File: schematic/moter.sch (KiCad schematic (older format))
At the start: 8 parts, among them J8 Conn_01x05, J9 Conn_01x05, U3 PCA9685PW

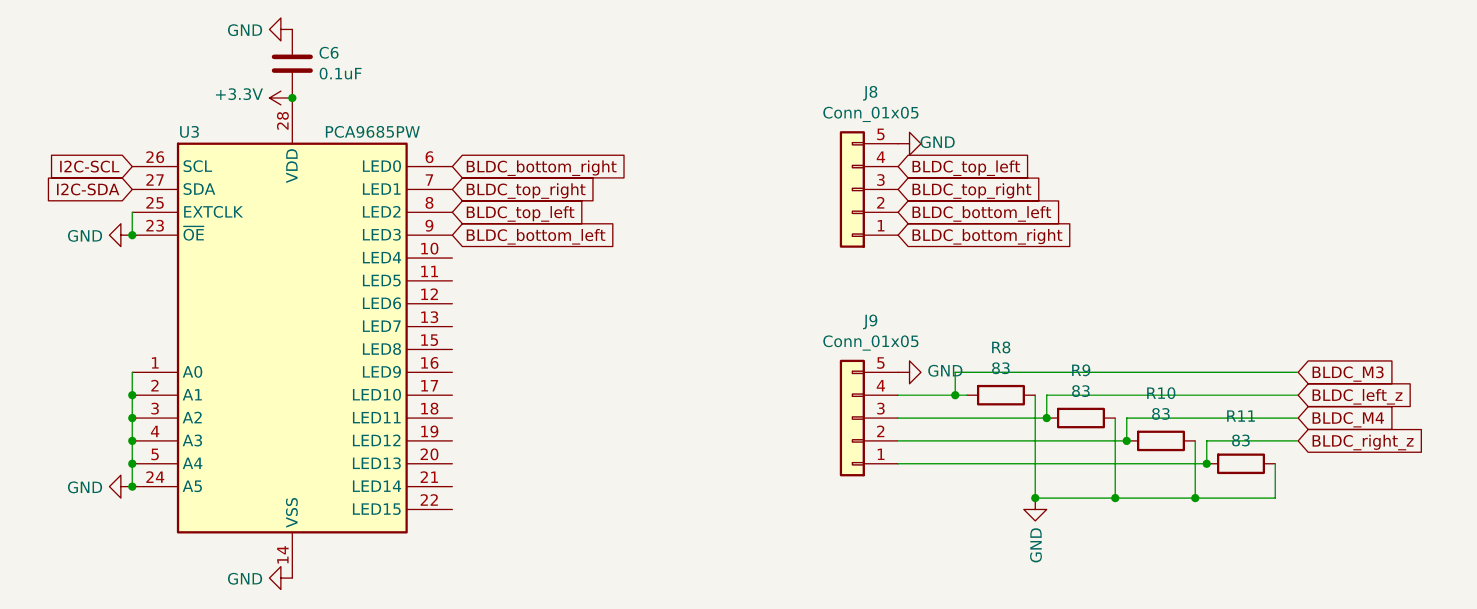
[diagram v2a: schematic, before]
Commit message: boost converter on Apsu board and PCB design
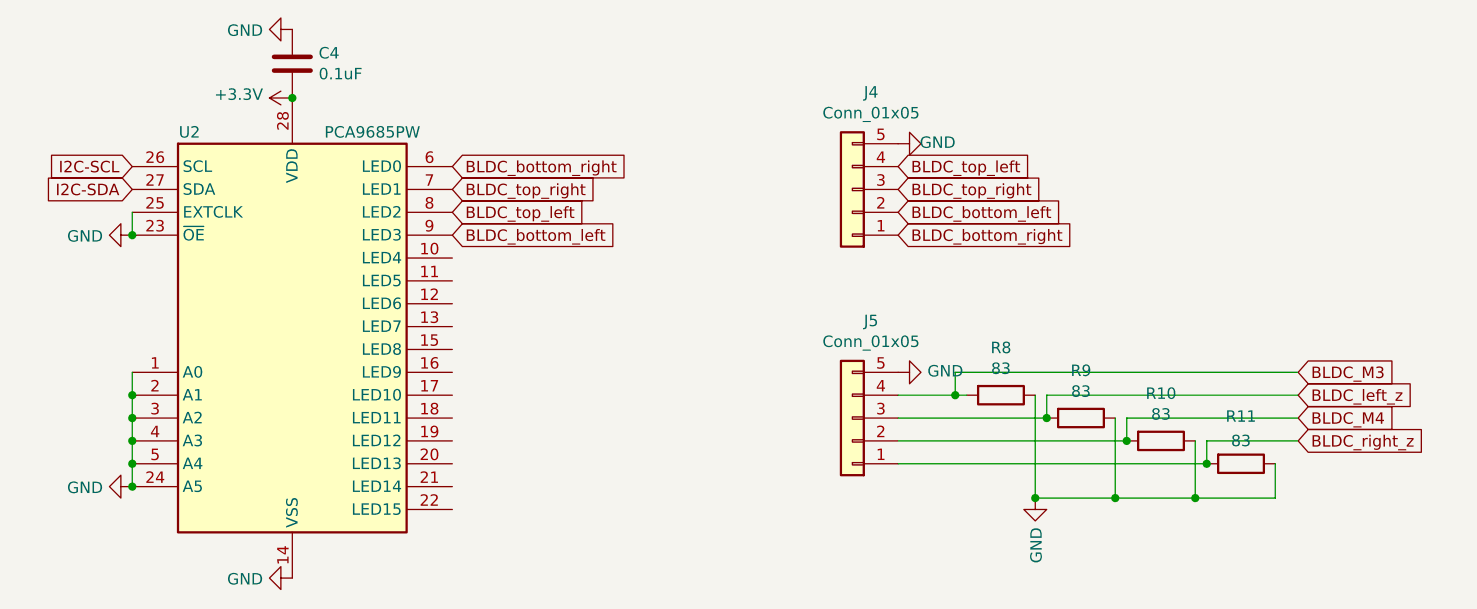
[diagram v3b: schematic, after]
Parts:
- renumbered C6 to C4, J8 to J4, J9 to J5, U3 to U2
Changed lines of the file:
@@
 $Descr A4 11693 8268
 encoding utf-8
-Sheet 4 5
+Sheet 3 5
 Title ""
 Date ""
@@
 P 2400 2550
 AR Path="/5EF432FA" Ref="U?"  Part="1"
-AR Path="/5EF07089/5EF432FA" Ref="U3"  Part="1"
-F 0 "U3" H 1950 3400 50  0000 C CNN
+AR Path="/5EF07089/5EF432FA" Ref="U2"  Part="1"
+F 0 "U2" H 1950 3400 50  0000 C CNN
 F 1 "PCA9685PW" H 2750 3400 50  0000 C CNN
 F 2 "Package_SO:TSSOP-28_4.4x9.7mm_P0.65mm" H 2425 1575 50  0001 L CNN
@@
 P 2400 1550
 AR Path="/5EF43302" Ref="#PWR?"  Part="1"
-AR Path="/5EF07089/5EF43302" Ref="#PWR031"  Part="1"
-F 0 "#PWR031" H 2400 1400 50  0001 C CNN
+AR Path="/5EF07089/5EF43302" Ref="#PWR022"  Part="1"
+F 0 "#PWR022" H 2400 1400 50  0001 C CNN
 F 1 "+3.3V" V 2415 1678 50  0000 L CNN
 F 2 "" H 2400 1550 50  0001 C CNN
@@
 P 2400 1400
 AR Path="/5EF43308" Ref="C?"  Part="1"
-AR Path="/5EF07089/5EF43308" Ref="C6"  Part="1"
-F 0 "C6" H 2515 1446 50  0000 L CNN
+AR Path="/5EF07089/5EF43308" Ref="C4"  Part="1"
+F 0 "C4" H 2515 1446 50  0000 L CNN
 F 1 "0.1uF" H 2515 1355 50  0000 L CNN
 F 2 "Capacitor_SMD:C_0805_2012Metric_Pad1.15x1.40mm_HandSolder" H 2438 1250 50  0001 C CNN
@@
 P 2400 3650
 AR Path="/5EF4330F" Ref="#PWR?"  Part="1"
-AR Path="/5EF07089/5EF4330F" Ref="#PWR032"  Part="1"
-F 0 "#PWR032" H 2400 3400 50  0001 C CNN
+AR Path="/5EF07089/5EF4330F" Ref="#PWR023"  Part="1"
+F 0 "#PWR023" H 2400 3400 50  0001 C CNN
 F 1 "GND" V 2405 3522 50  0000 R CNN
 F 2 "" H 2400 3650 50  0001 C CNN
@@
 P 1700 3250
 AR Path="/5EF4331F" Ref="#PWR?"  Part="1"
-AR Path="/5EF07089/5EF4331F" Ref="#PWR029"  Part="1"
-F 0 "#PWR029" H 1700 3000 50  0001 C CNN
+AR Path="/5EF07089/5EF4331F" Ref="#PWR020"  Part="1"
+F 0 "#PWR020" H 1700 3000 50  0001 C CNN
 F 1 "GND" V 1705 3122 50  0000 R CNN
 F 2 "" H 1700 3250 50  0001 C CNN
@@
 P 1700 2150
 AR Path="/5EF43326" Ref="#PWR?"  Part="1"
-AR Path="/5EF07089/5EF43326" Ref="#PWR028"  Part="1"
-F 0 "#PWR028" H 1700 1900 50  0001 C CNN
+AR Path="/5EF07089/5EF43326" Ref="#PWR019"  Part="1"
+F 0 "#PWR019" H 1700 1900 50  0001 C CNN
 F 1 "GND" V 1705 2022 50  0000 R CNN
 F 2 "" H 1700 2150 50  0001 C CNN
@@
 P 2400 1250
 AR Path="/5EF4332D" Ref="#PWR?"  Part="1"
-AR Path="/5EF07089/5EF4332D" Ref="#PWR030"  Part="1"
-F 0 "#PWR030" H 2400 1000 50  0001 C CNN
+AR Path="/5EF07089/5EF4332D" Ref="#PWR021"  Part="1"
+F 0 "#PWR021" H 2400 1000 50  0001 C CNN
 F 1 "GND" V 2405 1122 50  0000 R CNN
 F 2 "" H 2400 1250 50  0001 C CNN
@@
 P 5050 2750
 AR Path="/5EF64F4D" Ref="#PWR?"  Part="1"
-AR Path="/5EF07089/5EF64F4D" Ref="#PWR033"  Part="1"
-F 0 "#PWR033" H 5050 2500 50  0001 C CNN
+AR Path="/5EF07089/5EF64F4D" Ref="#PWR025"  Part="1"
+F 0 "#PWR025" H 5050 2500 50  0001 C CNN
 F 1 "GND" V 5055 2622 50  0000 R CNN
 F 2 "" H 5050 2750 50  0001 C CNN
@@
 	6050 2950 6800 2950
 $Comp
-L Connector_Generic:Conn_01x05 J8
+L Connector_Generic:Conn_01x05 J4
 U 1 1 5ED5189E
 P 4850 1950
-F 0 "J8" H 4768 1525 50  0000 C CNN
+F 0 "J4" H 4768 1525 50  0000 C CNN
 F 1 "Conn_01x05" H 4768 1616 50  0000 C CNN
 F 2 "Connector_JST:JST_XH_B5B-XH-A_1x05_P2.50mm_Vertical" H 4850 1950 50  0001 C CNN
@@
 P 5050 1750
 AR Path="/5ED56EC8" Ref="#PWR?"  Part="1"
-AR Path="/5EF07089/5ED56EC8" Ref="#PWR0101"  Part="1"
-F 0 "#PWR0101" H 5050 1500 50  0001 C CNN
+AR Path="/5EF07089/5ED56EC8" Ref="#PWR024"  Part="1"
+F 0 "#PWR024" H 5050 1500 50  0001 C CNN
 F 1 "GND" V 5055 1577 50  0000 C CNN
 F 2 "" H 5050 1750 50  0001 C CNN
@@
 $EndComp
 $Comp
-L Connector_Generic:Conn_01x05 J9
+L Connector_Generic:Conn_01x05 J5
 U 1 1 5EE5CFE9
 P 4850 2950
-F 0 "J9" H 4768 2525 50  0000 C CNN
+F 0 "J5" H 4768 2525 50  0000 C CNN
 F 1 "Conn_01x05" H 4768 2616 50  0000 C CNN
 F 2 "Connector_JST:JST_XH_B5B-XH-A_1x05_P2.50mm_Vertical" H 4850 2950 50  0001 C CNN
@@
 P 5650 3300
 AR Path="/5EED624C" Ref="#PWR?"  Part="1"
-AR Path="/5EF07089/5EED624C" Ref="#PWR0102"  Part="1"
-F 0 "#PWR0102" H 5650 3050 50  0001 C CNN
+AR Path="/5EF07089/5EED624C" Ref="#PWR026"  Part="1"
+F 0 "#PWR026" H 5650 3050 50  0001 C CNN
 F 1 "GND" V 5655 3172 50  0000 R CNN
 F 2 "" H 5650 3300 50  0001 C CNN

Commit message: new components on pcb
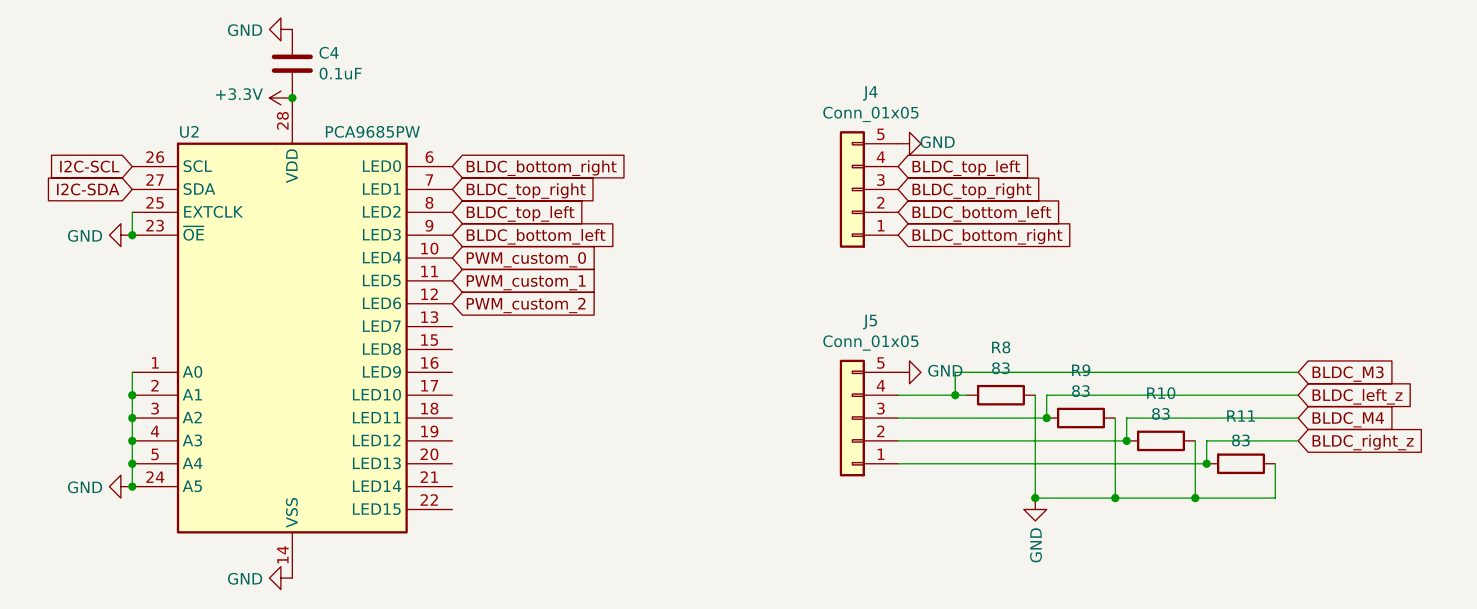
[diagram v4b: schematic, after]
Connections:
- net PWM_custom_0: now reaches U2.10 (LED4)
- net PWM_custom_1: now reaches U2.11 (LED5)
- net PWM_custom_2: now reaches U2.12 (LED6)
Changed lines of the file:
@@
 $EndComp
 Connection ~ 5650 3300
+Text GLabel 3100 2250 2    50   Input ~ 0
+PWM_custom_0
+Text GLabel 3100 2350 2    50   Input ~ 0
+PWM_custom_1
+Text GLabel 3100 2450 2    50   Input ~ 0
+PWM_custom_2
 $EndSCHEMATC

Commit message: JTAG anti-ring resistors
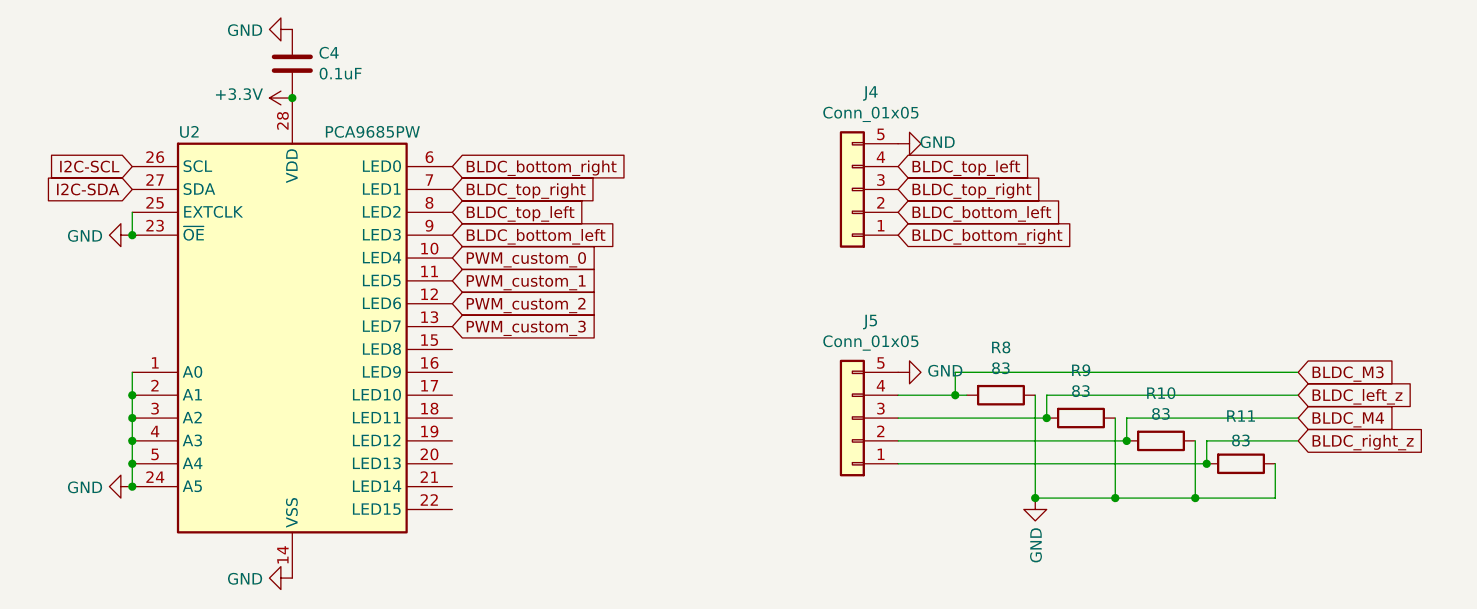
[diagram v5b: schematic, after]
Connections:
- net PWM_custom_3: now reaches U2.13 (LED7)
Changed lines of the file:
@@
 Connection ~ 1700 2850
 Wire Wire Line
-	1700 2950 1700 3050
-Connection ~ 1700 2950
-Wire Wire Line
-	1700 3050 1700 3150
-Connection ~ 1700 3050
-Wire Wire Line
 	1700 3150 1700 3250
-Connection ~ 1700 3150
 $Comp
 L power:GND #PWR?
@@
 Text GLabel 3100 2450 2    50   Input ~ 0
 PWM_custom_2
+Text GLabel 3100 2550 2    50   Input ~ 0
+PWM_custom_3
+Connection ~ 1700 3150
+Wire Wire Line
+	1700 3050 1700 3150
+Connection ~ 1700 3050
+Connection ~ 1700 2950
+Wire Wire Line
+	1700 2950 1700 3050
 $EndSCHEMATC

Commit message: wireing
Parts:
- U2: footprint Package_SO:TSSOP-28_4.4x9.7mm_P0.65mm -> PCA9685:NXP_Semiconductors-SOT788-1-02_2016-0-MFG
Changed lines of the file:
@@
 F 0 "U2" H 1950 3400 50  0000 C CNN
 F 1 "PCA9685PW" H 2750 3400 50  0000 C CNN
-F 2 "Package_SO:TSSOP-28_4.4x9.7mm_P0.65mm" H 2425 1575 50  0001 L CNN
+F 2 "PCA9685:NXP_Semiconductors-SOT788-1-02_2016-0-MFG" H 2425 1575 50  0001 L CNN
 F 3 "http://www.nxp.com/documents/data_sheet/PCA9685.pdf" H 2000 3250 50  0001 C CNN
 	1    2400 2550

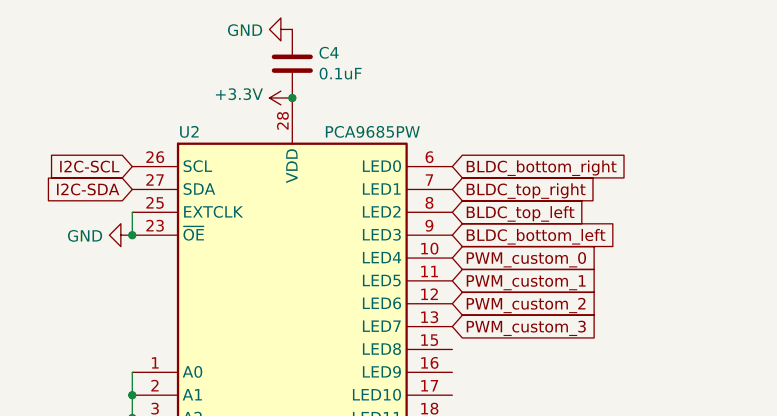
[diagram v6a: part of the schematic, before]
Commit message: added MPN
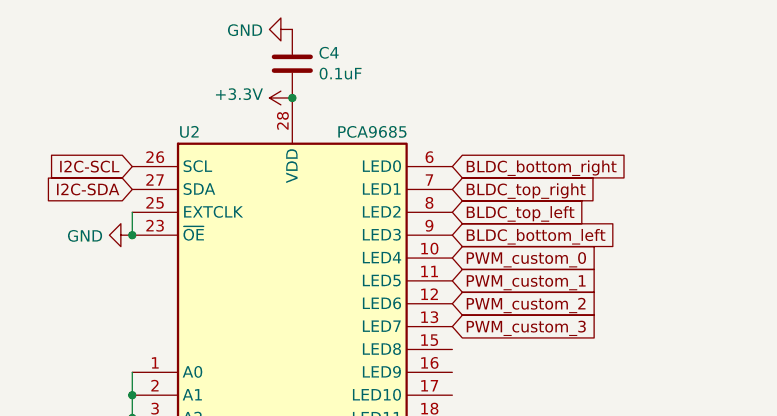
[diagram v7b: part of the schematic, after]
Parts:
- C4: MPN (none) -> C0805C104J5RACTU
- R10, R11, R8, R9: MPN (none) -> ERA-6AEB820V
- U2: value PCA9685PW -> PCA9685; MPN (none) -> PCA9685BS,118

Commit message: added MPN for connectors
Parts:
- J4, J5: MPN (none) -> B5B-XH-A(LF)(SN)
